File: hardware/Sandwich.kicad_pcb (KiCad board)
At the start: 2 copper layers, 80 x 70 mm, 24 parts, among them P1 CONN_01X20, P2 CONN_01X06, P3 VGA_OUT, Q1 PZT2222A, U1 P8X32A-D40, U2 24C512, Y1 5MHz

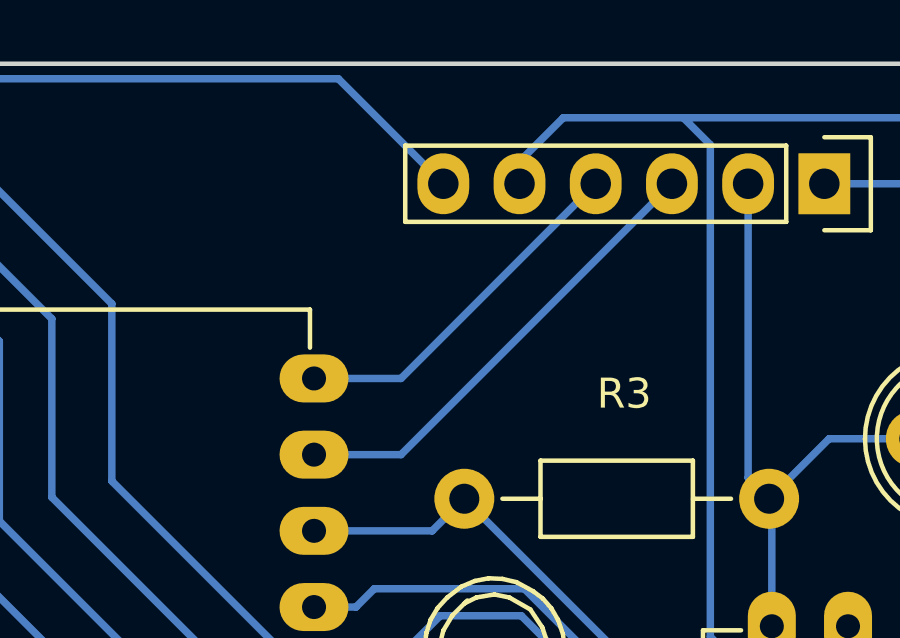
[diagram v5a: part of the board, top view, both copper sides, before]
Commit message: TX/RX pins were switched over. Regenerated PCB and everything else.
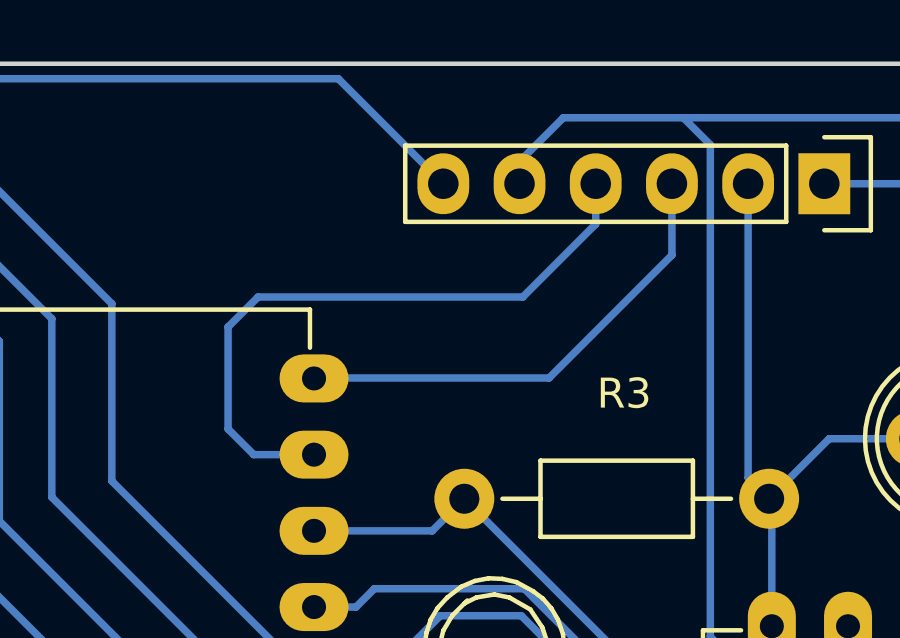
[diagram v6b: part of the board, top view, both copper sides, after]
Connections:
- U1 pad 39: PROP_TX -> PROP_RX
- U1 pad 40: PROP_RX -> PROP_TX
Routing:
- net PROP_RX: track 12.1 -> 22.3 mm
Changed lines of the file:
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@@
-(kicad_pcb (version 4) (host pcbnew 4.0.2-4+6225~38~ubuntu14.04.1-stable)
+(kicad_pcb (version 4) (host pcbnew "(2016-02-14 BZR 6556)-product")
   (general
     (links 70)
     (no_connects 1)
-    (area 12.011474 14.3745 100.893001 88.47626)
+    (area 14.924999 15.924999 95.075001 86.075001)
     (thickness 1.6)
     (drawings 6)
-    (tracks 230)
+    (tracks 237)
     (zones 0)
     (modules 24)
@@
       (hpglpenspeed 20)
       (hpglpendiameter 15)
-      (hpglpenoverlay 2)
       (psnegative false)
       (psa4output false)
@@
       (net 37 "Net-(R3-Pad1)"))
     (pad 39 thru_hole oval (at 15.24 2.54) (size 2.3 1.6) (drill 0.8) (layers *.Cu *.Mask F.SilkS)
+      (net 23 PROP_RX))
+    (pad 40 thru_hole oval (at 15.24 0) (size 2.3 1.6) (drill 0.8) (layers *.Cu *.Mask F.SilkS)
       (net 50 PROP_TX))
-    (pad 40 thru_hole oval (at 15.24 0) (size 2.3 1.6) (drill 0.8) (layers *.Cu *.Mask F.SilkS)
-      (net 23 PROP_RX))
     (model Housings_DIP.3dshapes/DIP-40_W15.24mm_LongPads.wrl
       (at (xyz 0 0 0))
@@
   (segment (start 48.5 25.25) (end 48.5 31.24) (width 0.25) (layer B.Cu) (net 22))
   (segment (start 48.5 31.24) (end 58.99 41.73) (width 0.25) (layer B.Cu) (net 22))
-  (segment (start 58.99 26.49) (end 61.89 26.49) (width 0.25) (layer B.Cu) (net 23))
-  (segment (start 61.89 26.49) (end 68.38 20) (width 0.25) (layer B.Cu) (net 23))
+  (segment (start 68.38 20) (end 68.38 21.345) (width 0.25) (layer B.Cu) (net 23) (status 400000))
+  (segment (start 56.98 29.03) (end 58.99 29.03) (width 0.25) (layer B.Cu) (net 23) (status 800000))
+  (segment (start 56.125 28.175) (end 56.98 29.03) (width 0.25) (layer B.Cu) (net 23))
+  (segment (start 56.125 24.775) (end 56.125 28.175) (width 0.25) (layer B.Cu) (net 23))
+  (segment (start 57.125 23.775) (end 56.125 24.775) (width 0.25) (layer B.Cu) (net 23))
+  (segment (start 65.95 23.775) (end 57.125 23.775) (width 0.25) (layer B.Cu) (net 23))
+  (segment (start 68.38 21.345) (end 65.95 23.775) (width 0.25) (layer B.Cu) (net 23))
+  (segment (start 58.99 29.03) (end 58.28 29.03) (width 0.25) (layer B.Cu) (net 23))
   (segment (start 25.5 26.49) (end 31.51 26.49) (width 0.25) (layer B.Cu) (net 24))
   (segment (start 31.51 26.49) (end 40.25 17.75) (width 0.25) (layer B.Cu) (net 24))
@@
   (segment (start 50.25 24.5) (end 50.25 30.45) (width 0.25) (layer B.Cu) (net 49))
   (segment (start 50.25 30.45) (end 58.99 39.19) (width 0.25) (layer B.Cu) (net 49))
-  (segment (start 58.99 29.03) (end 61.89 29.03) (width 0.25) (layer B.Cu) (net 50))
-  (segment (start 61.89 29.03) (end 70.92 20) (width 0.25) (layer B.Cu) (net 50))
-  (segment (start 58.99 29.03) (end 58.28 29.03) (width 0.25) (layer B.Cu) (net 50))
+  (segment (start 70.92 20) (end 70.92 22.38) (width 0.25) (layer B.Cu) (net 50) (status 400000))
+  (segment (start 66.825 26.475) (end 59.005 26.475) (width 0.25) (layer B.Cu) (net 50) (status 800000))
+  (segment (start 70.92 22.38) (end 66.825 26.475) (width 0.25) (layer B.Cu) (net 50))
+  (segment (start 59.005 26.475) (end 58.99 26.49) (width 0.25) (layer B.Cu) (net 50) (status C00000))
 )

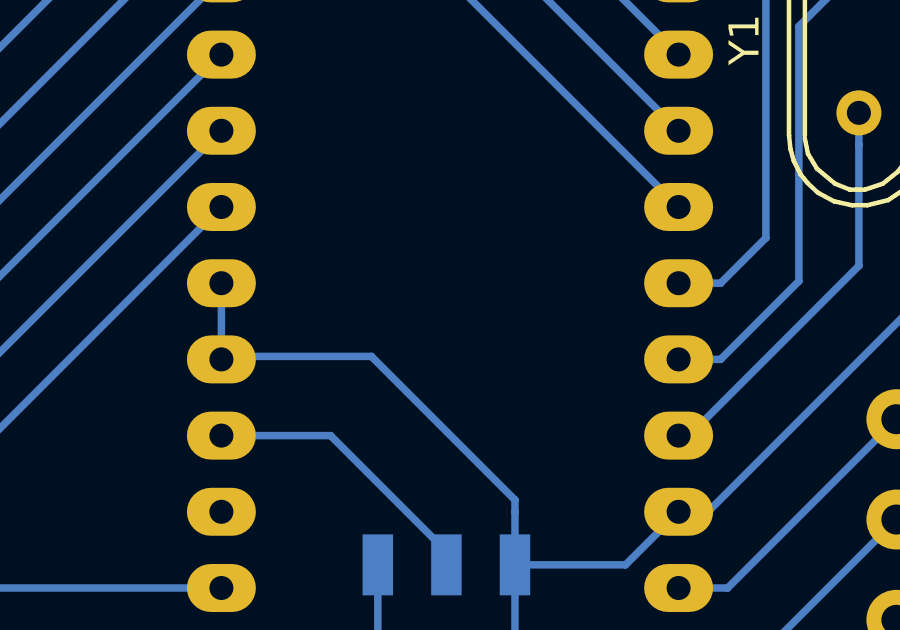
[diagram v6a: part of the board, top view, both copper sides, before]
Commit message: Added a cap.
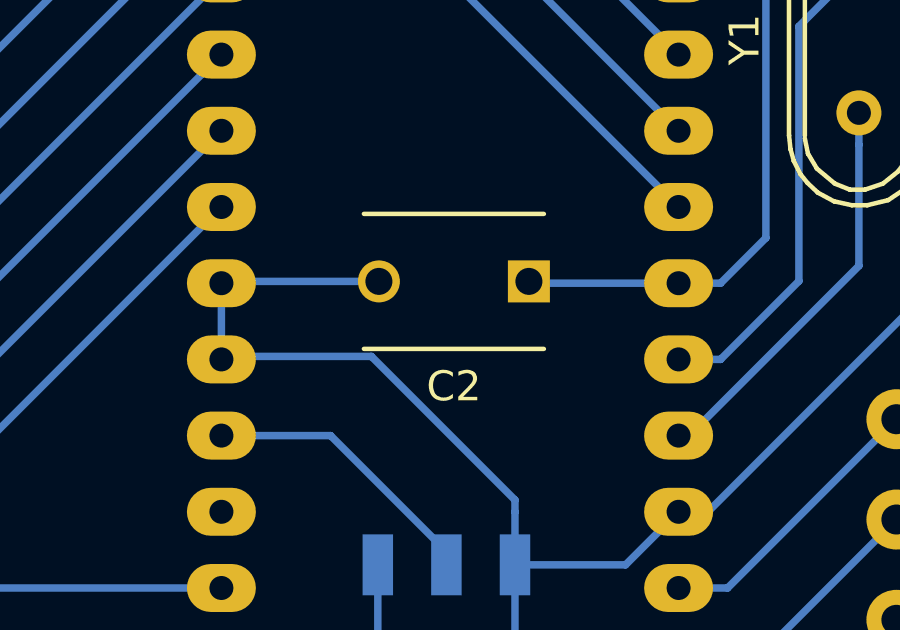
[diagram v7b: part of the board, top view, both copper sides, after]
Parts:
- added C2: 100nF, Capacitors_ThroughHole:C_Disc_D6_P5, F.Cu at (54.0, 46.8)
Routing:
- net GND: track 272.1 -> 277.4 mm
- net 3.3V: track 73.1 -> 78.1 mm
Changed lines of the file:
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@@
 (kicad_pcb (version 4) (host pcbnew "(2016-02-14 BZR 6556)-product")
   (general
-    (links 70)
+    (links 72)
     (no_connects 1)
-    (area 14.924999 15.924999 95.075001 86.075001)
+    (area 12.011474 14.3745 100.893001 88.47626)
     (thickness 1.6)
     (drawings 6)
-    (tracks 237)
+    (tracks 241)
     (zones 0)
-    (modules 24)
+    (modules 25)
     (nets 51)
   )
@@
     (visible_elements 7FFFFFFF)
     (pcbplotparams
-      (layerselection 0x00000_80000000)
+      (layerselection 0x00000_fffffffe)
       (usegerberextensions false)
       (excludeedgelayer true)
@@
     (pad 1 thru_hole circle (at 0 0) (size 3 3) (drill 3) (layers))
   )
+  (module Capacitors_ThroughHole:C_Disc_D6_P5 (layer F.Cu)
+    (at 54 46.75 180)
+    (descr "Capacitor 6mm Disc, Pitch 5mm")
+    (tags Capacitor)
+    (fp_text reference C2 (at 2.5 -3.5 180) (layer F.SilkS)
+      (effects (font (size 1 1) (thickness 0.15)))
+    )
+    (fp_text value 100nF (at 2.5 3.5 180) (layer F.Fab)
+      (effects (font (size 1 1) (thickness 0.15)))
+    )
+    (fp_line (start -0.95 -2.5) (end 5.95 -2.5) (layer F.CrtYd) (width 0.05))
+    (fp_line (start 5.95 -2.5) (end 5.95 2.5) (layer F.CrtYd) (width 0.05))
+    (fp_line (start 5.95 2.5) (end -0.95 2.5) (layer F.CrtYd) (width 0.05))
+    (fp_line (start -0.95 2.5) (end -0.95 -2.5) (layer F.CrtYd) (width 0.05))
+    (fp_line (start -0.5 -2.25) (end 5.5 -2.25) (layer F.SilkS) (width 0.15))
+    (fp_line (start 5.5 2.25) (end -0.5 2.25) (layer F.SilkS) (width 0.15))
+    (pad 1 thru_hole rect (at 0 0 180) (size 1.4 1.4) (drill 0.9) (layers *.Cu *.Mask F.SilkS)
+      (net 4 3.3V))
+    (pad 2 thru_hole circle (at 5 0 180) (size 1.4 1.4) (drill 0.9) (layers *.Cu *.Mask F.SilkS)
+      (net 26 GND))
+    (model Capacitors_ThroughHole.3dshapes/C_Disc_D6_P5.wrl
+      (at (xyz 0.0984252 0 0))
+      (scale (xyz 1 1 1))
+      (rotate (xyz 0 0 0))
+    )
+  )
   (gr_line (start 15 86) (end 16 86) (angle 90) (layer Edge.Cuts) (width 0.15))
   (gr_line (start 15 16) (end 15 86) (angle 90) (layer Edge.Cuts) (width 0.15))
@@
   (segment (start 84.913492 28.5) (end 82.74 28.5) (width 0.25) (layer B.Cu) (net 3))
   (segment (start 82.74 28.5) (end 81.54 28.5) (width 0.25) (layer B.Cu) (net 3))
+  (segment (start 58.99 46.81) (end 54.06 46.81) (width 0.25) (layer B.Cu) (net 4) (status C00000))
+  (segment (start 54.06 46.81) (end 54 46.75) (width 0.25) (layer B.Cu) (net 4) (status C00000))
   (segment (start 79 28.5) (end 79 30.1) (width 0.25) (layer B.Cu) (net 4))
   (segment (start 85 36.4) (end 82.1 39.3) (width 0.25) (layer B.Cu) (net 4))
@@
   (segment (start 48.5 25.25) (end 48.5 31.24) (width 0.25) (layer B.Cu) (net 22))
   (segment (start 48.5 31.24) (end 58.99 41.73) (width 0.25) (layer B.Cu) (net 22))
-  (segment (start 68.38 20) (end 68.38 21.345) (width 0.25) (layer B.Cu) (net 23) (status 400000))
-  (segment (start 56.98 29.03) (end 58.99 29.03) (width 0.25) (layer B.Cu) (net 23) (status 800000))
+  (segment (start 68.38 20) (end 68.38 21.345) (width 0.25) (layer B.Cu) (net 23))
+  (segment (start 56.98 29.03) (end 58.99 29.03) (width 0.25) (layer B.Cu) (net 23))
   (segment (start 56.125 28.175) (end 56.98 29.03) (width 0.25) (layer B.Cu) (net 23))
   (segment (start 56.125 24.775) (end 56.125 28.175) (width 0.25) (layer B.Cu) (net 23))
@@
   (segment (start 92.1 48.8) (end 92.1 25.5) (width 0.25) (layer B.Cu) (net 25))
   (segment (start 92.1 25.5) (end 86.6 20) (width 0.25) (layer B.Cu) (net 25))
+  (segment (start 49 46.75) (end 43.81 46.75) (width 0.25) (layer B.Cu) (net 26) (status C00000))
+  (segment (start 43.81 46.75) (end 43.75 46.81) (width 0.25) (layer B.Cu) (net 26) (status C00000))
   (segment (start 64.25 78.75) (end 77.05 78.75) (width 0.25) (layer B.Cu) (net 26))
   (segment (start 86.7 17.8) (end 71.3 17.8) (width 0.25) (layer B.Cu) (net 26))
@@
   (segment (start 50.25 24.5) (end 50.25 30.45) (width 0.25) (layer B.Cu) (net 49))
   (segment (start 50.25 30.45) (end 58.99 39.19) (width 0.25) (layer B.Cu) (net 49))
-  (segment (start 70.92 20) (end 70.92 22.38) (width 0.25) (layer B.Cu) (net 50) (status 400000))
-  (segment (start 66.825 26.475) (end 59.005 26.475) (width 0.25) (layer B.Cu) (net 50) (status 800000))
+  (segment (start 70.92 20) (end 70.92 22.38) (width 0.25) (layer B.Cu) (net 50))
+  (segment (start 66.825 26.475) (end 59.005 26.475) (width 0.25) (layer B.Cu) (net 50))
   (segment (start 70.92 22.38) (end 66.825 26.475) (width 0.25) (layer B.Cu) (net 50))
-  (segment (start 59.005 26.475) (end 58.99 26.49) (width 0.25) (layer B.Cu) (net 50) (status C00000))
+  (segment (start 59.005 26.475) (end 58.99 26.49) (width 0.25) (layer B.Cu) (net 50))
 )
